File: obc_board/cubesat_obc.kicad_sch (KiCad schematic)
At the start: 22 parts

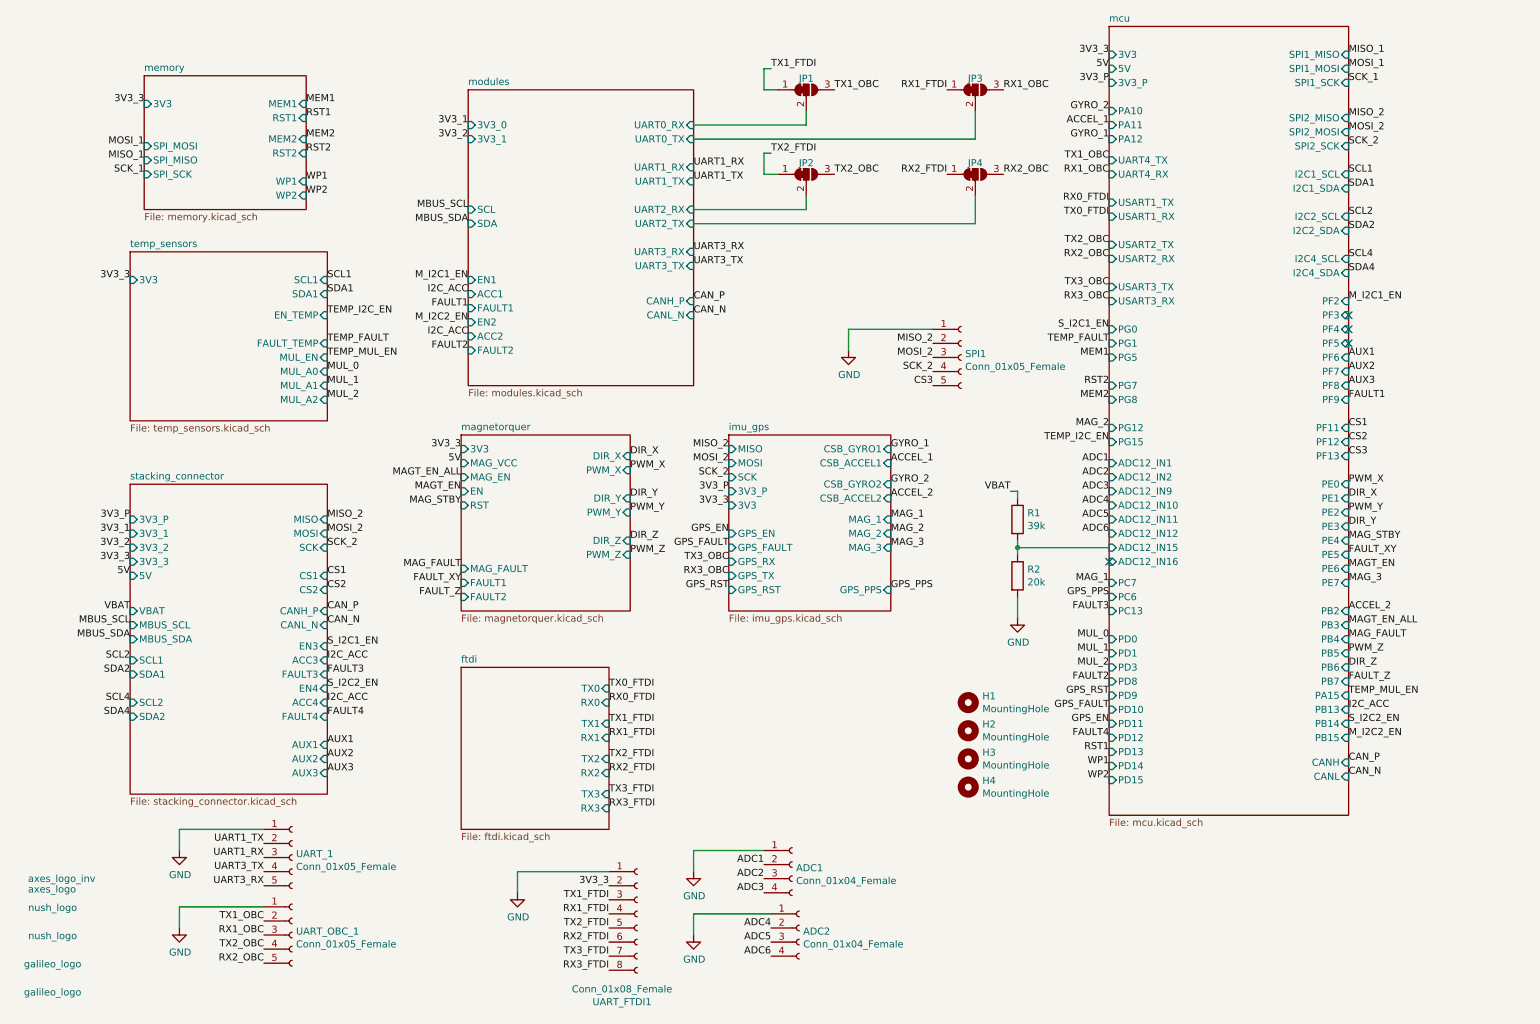
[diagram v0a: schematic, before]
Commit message: changed picoblade symbols to include mounting pins, added photodiode circuitry and additional testpoints, added GPS to FTDI jumper
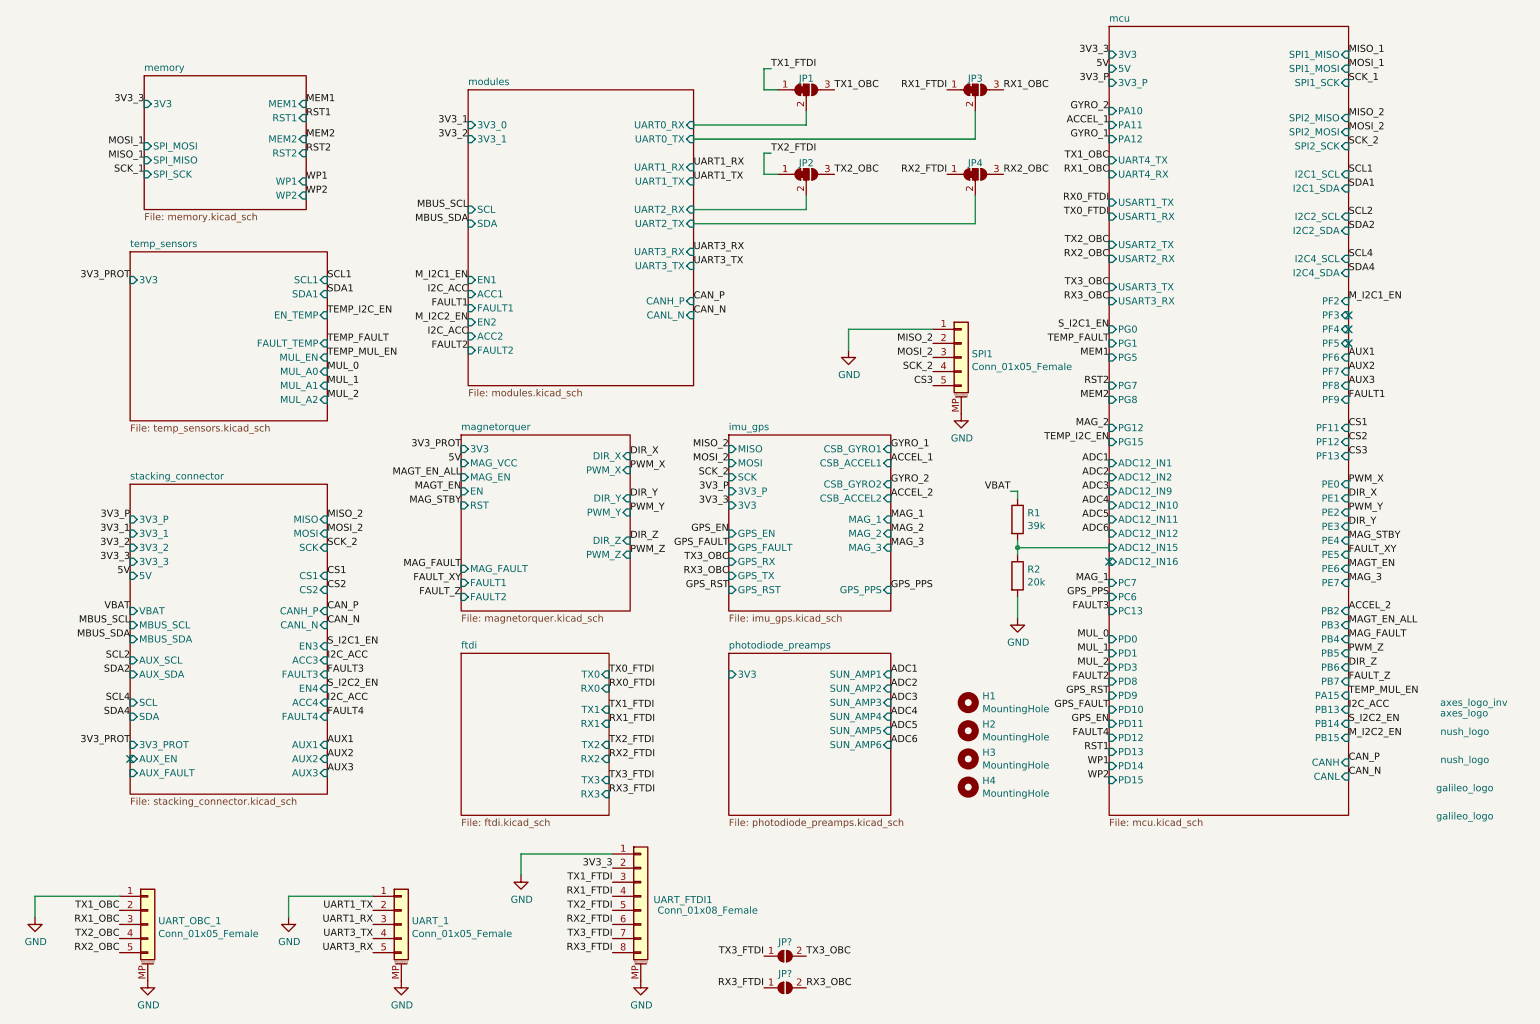
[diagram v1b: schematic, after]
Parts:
- removed ADC1, ADC2: Conn_01x04_Female, Connector_Molex:Molex_PicoBlade_53261-0471_1x04-1MP_P1.25mm_Horizontal, symbol Connector:Conn_01x04_Female
- added JP? (x2): SolderJumper_2_Open, symbol Jumper:SolderJumper_2_Open
- SPI1, UART_1, UART_OBC_1: symbol Connector:Conn_01x05_Female -> Connector_Generic_MountingPin:Conn_01x05_MountingPin
- UART_FTDI1: symbol Connector:Conn_01x08_Female -> Connector_Generic_MountingPin:Conn_01x08_MountingPin
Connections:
- net GND: now also SPI1.MP (MountPin), UART_1.MP (MountPin), UART_FTDI1.MP (MountPin), UART_OBC_1.MP (MountPin)
- net RX3_FTDI: now also JP?.1 (A)
- net RX3_OBC: now also JP?.2 (B)
- net TX3_FTDI: now also JP?.1 (A)
- net TX3_OBC: now also JP?.2 (B)
- no-connect marks 4 -> 5
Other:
- added sheet photodiode_preamps (photodiode_preamps.kicad_sch)
- sheet stacking_connector ports: added 3V3_PROT, AUX_EN, AUX_FAULT, AUX_SCL, AUX_SDA, SCL, SDA; removed SCL1, SCL2, SDA1, SDA2

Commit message: updated footprints
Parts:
- JP? (x2): footprint (none) -> Jumper:SolderJumper-2_P1.3mm_Open_RoundedPad1.0x1.5mm

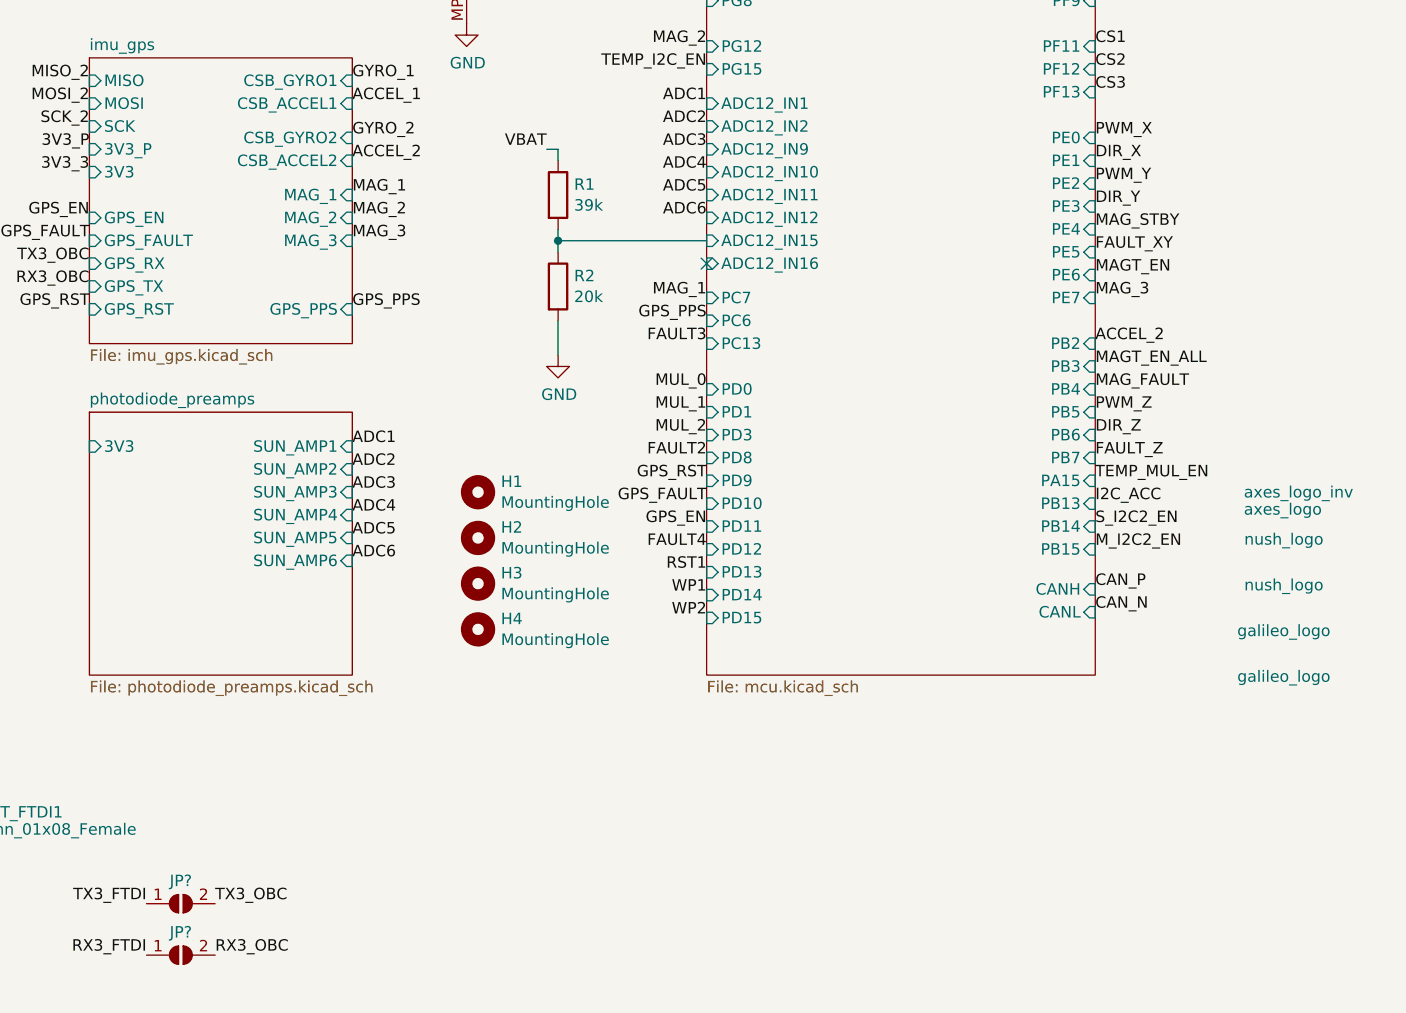
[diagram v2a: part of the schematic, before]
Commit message: remapped magnetorquer pins, routed tespoints
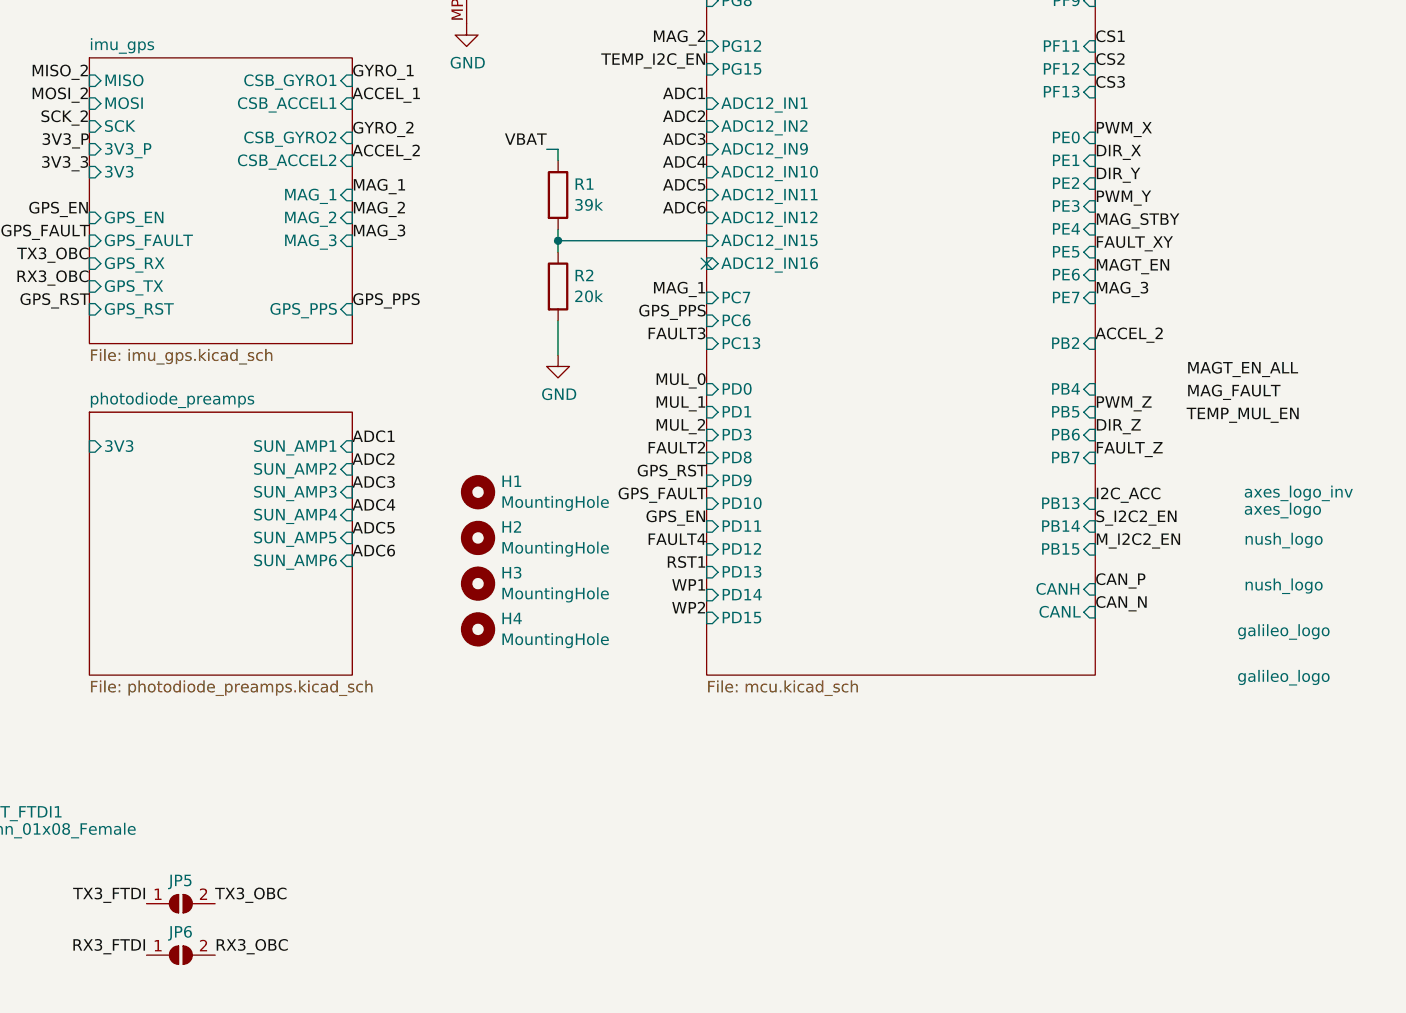
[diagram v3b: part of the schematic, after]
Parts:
- gave numbers to parts that had none: 2
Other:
- sheet mcu ports: added none; removed PA15, PB3

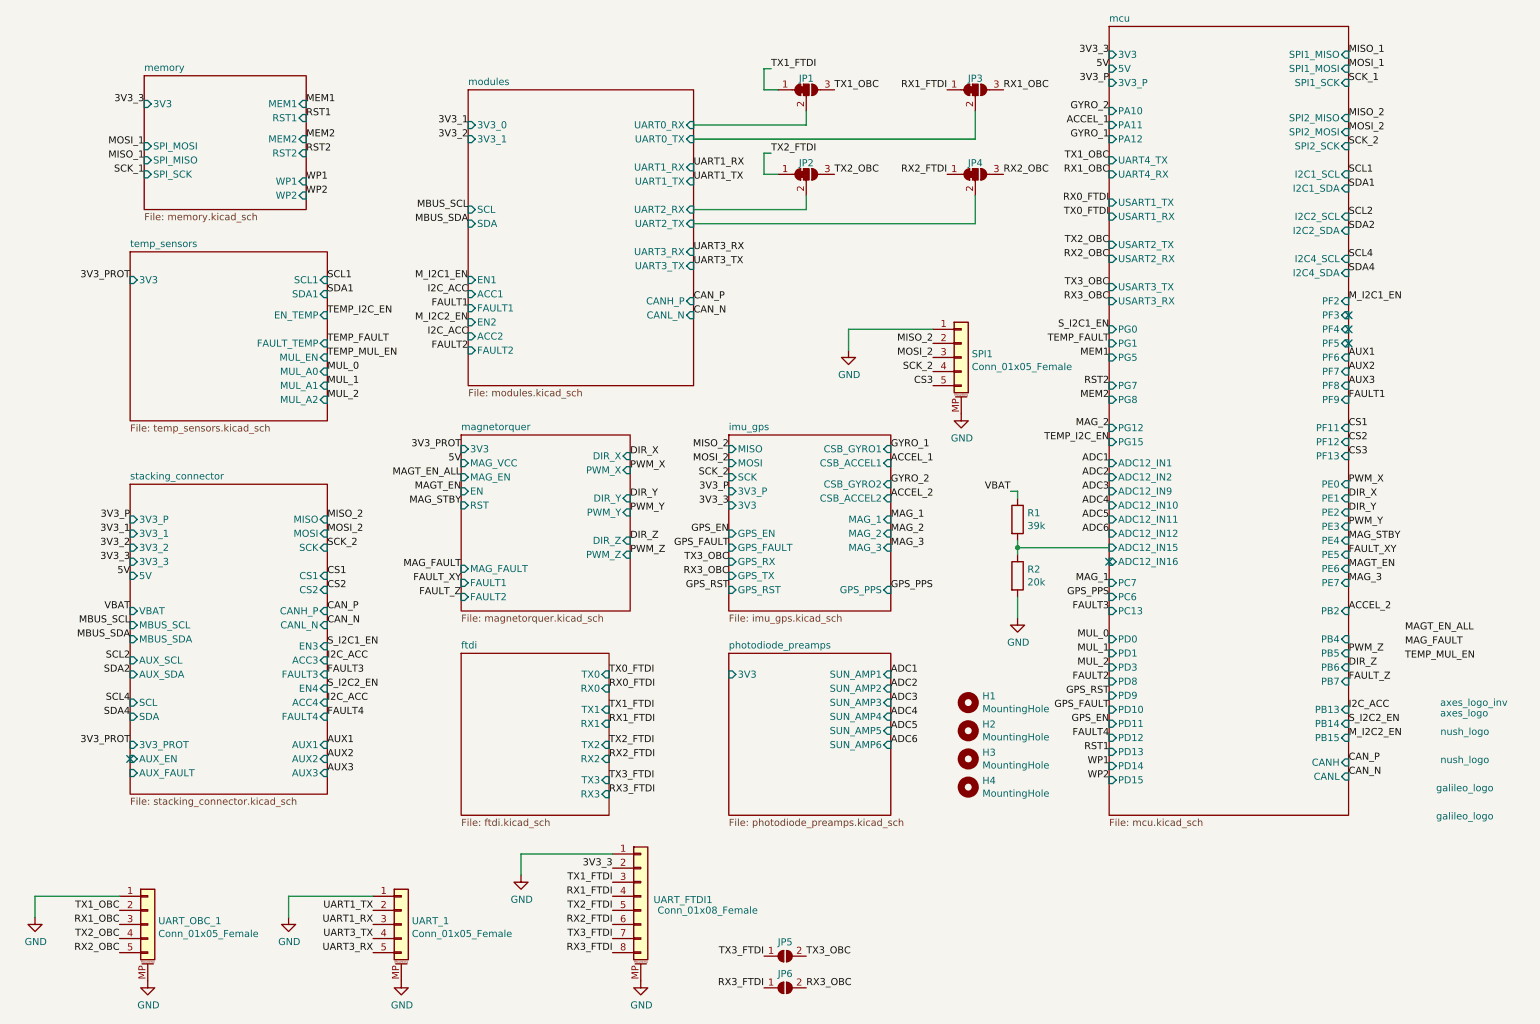
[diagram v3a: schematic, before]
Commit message: routed photodiode circuits, jtag and short circuit prot circuits
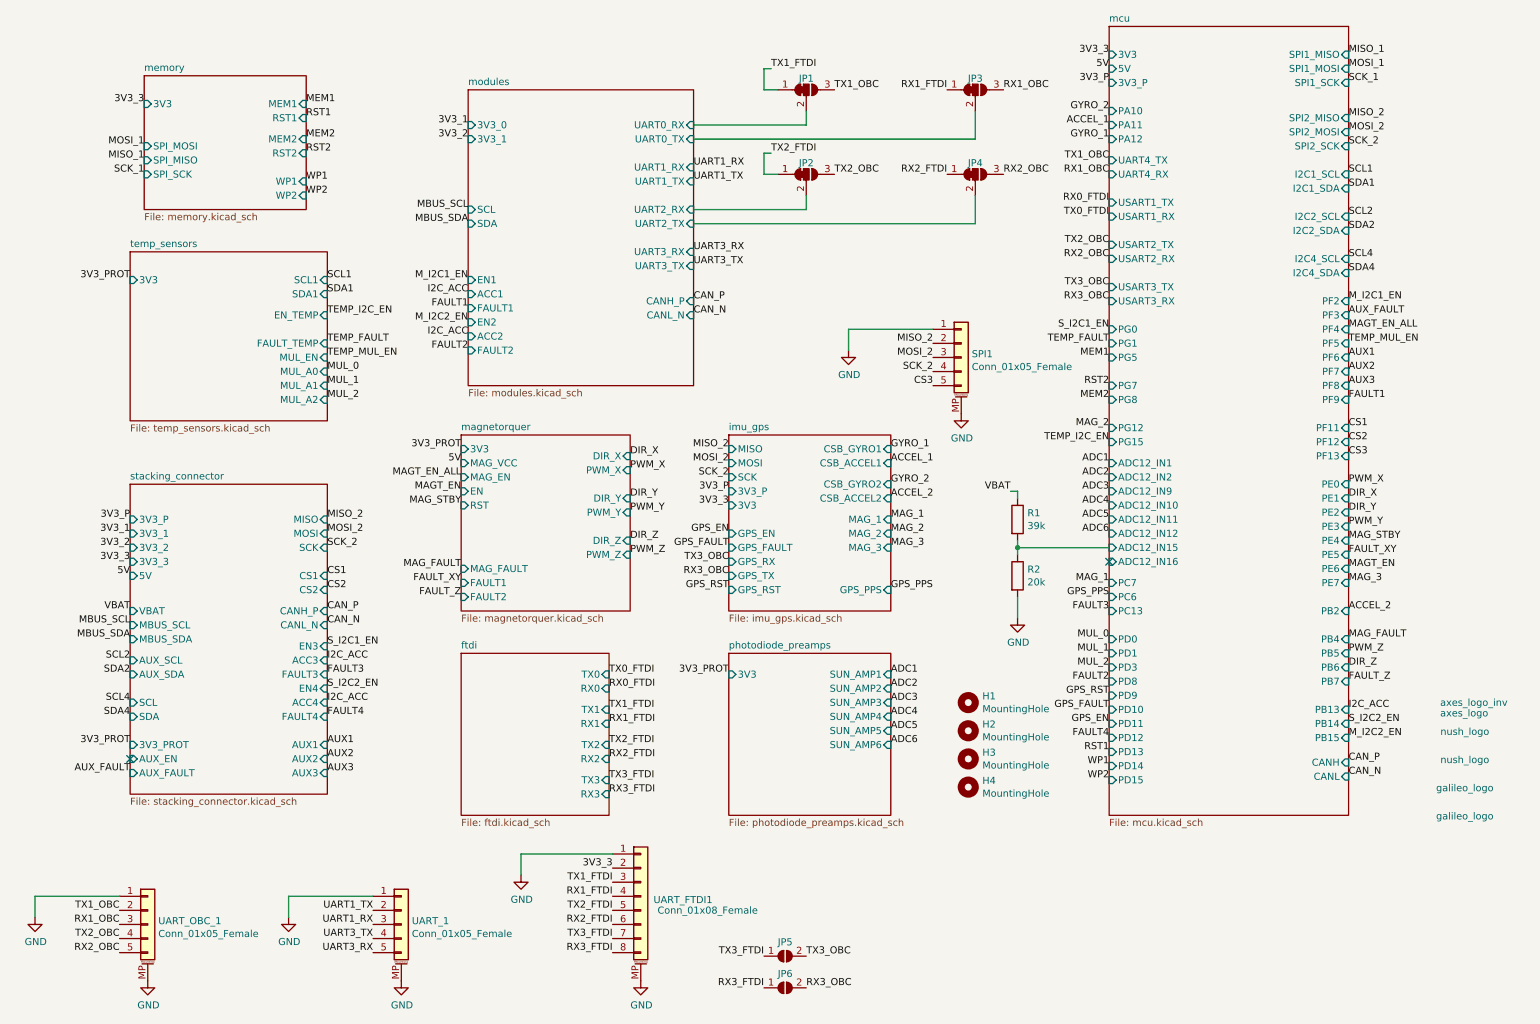
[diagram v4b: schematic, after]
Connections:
- no-connect marks 5 -> 2
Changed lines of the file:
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@@
   (no_connect (at 210.82 114.3))
   (no_connect (at 34.29 149.86))
-  (no_connect (at 254 69.85))
-  (no_connect (at 254 72.39))
-  (no_connect (at 254 74.93))
   (wire (pts (xy 186.69 53.34) (xy 186.69 48.26))
     (stroke (width 0) (type default) (color 0 0 0 0))
@@
     (effects (font (size 1.27 1.27)) (justify left bottom))
   )
+  (label "AUX_FAULT" (at 254 69.85 0)
+    (effects (font (size 1.27 1.27)) (justify left bottom))
+  )
   (label "DIR_Y" (at 124.46 102.87 0)
     (effects (font (size 1.27 1.27)) (justify left bottom))
@@
     (effects (font (size 1.27 1.27)) (justify right bottom))
   )
-  (label "TEMP_MUL_EN" (at 264.16 132.08 0)
+  (label "TEMP_MUL_EN" (at 254 74.93 0)
     (effects (font (size 1.27 1.27)) (justify left bottom))
   )
@@
     (effects (font (size 1.27 1.27)) (justify left bottom))
   )
-  (label "MAGT_EN_ALL" (at 264.16 127 0)
+  (label "MAGT_EN_ALL" (at 254 72.39 0)
     (effects (font (size 1.27 1.27)) (justify left bottom))
   )
@@
     (effects (font (size 1.27 1.27)) (justify left bottom))
   )
+  (label "3V3_PROT" (at 142.24 134.62 180)
+    (effects (font (size 1.27 1.27)) (justify right bottom))
+  )
   (label "3V3_2" (at 95.25 38.1 180)
     (effects (font (size 1.27 1.27)) (justify right bottom))
@@
     (effects (font (size 1.27 1.27)) (justify right bottom))
   )
-  (label "MAG_FAULT" (at 264.16 129.54 0)
+  (label "MAG_FAULT" (at 254 128.27 0)
     (effects (font (size 1.27 1.27)) (justify left bottom))
   )
@@
   )
   (label "3V3_1" (at 95.25 35.56 180)
+    (effects (font (size 1.27 1.27)) (justify right bottom))
+  )
+  (label "AUX_FAULT" (at 34.29 152.4 180)
     (effects (font (size 1.27 1.27)) (justify right bottom))
   )
@@
       (reference "C43") (unit 1) (value "1u") (footprint "Capacitor_SMD:C_0603_1608Metric")
     )
-    (path "/00000000-0000-0000-0000-00005f45b718/518297ee-c838-49ea-9874-b3ca5cdfc781"
-      (reference "C45") (unit 1) (value "10u") (footprint "Capacitor_SMD:C_1206_3216Metric")
-    )
     (path "/00000000-0000-0000-0000-00005fc7207b/00000000-0000-0000-0000-00005fcc2d83"
       (reference "C46") (unit 1) (value "22u") (footprint "Capacitor_SMD:C_1210_3225Metric")
@@
       (reference "JP6") (unit 1) (value "SolderJumper_2_Open") (footprint "Jumper:SolderJumper-2_P1.3mm_Open_RoundedPad1.0x1.5mm")
     )
+    (path "/00000000-0000-0000-0000-00005e7ec636/a5d17137-bbc9-4945-83bb-f3dee83c5671"
+      (reference "JP7") (unit 1) (value "Jumper_2_Open") (footprint "Jumper:SolderJumper-2_P1.3mm_Open_RoundedPad1.0x1.5mm")
+    )
     (path "/00000000-0000-0000-0000-00005f315fb6/00000000-0000-0000-0000-00005f3a4de3"
